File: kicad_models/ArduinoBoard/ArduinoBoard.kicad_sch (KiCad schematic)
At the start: 21 parts, among them J1 5V Output, J2 Buttons, J3 PWM Output, J4 12V Input, J5 Conn_01x04_Pin, J6 Conn_01x04_Pin, J7 Conn_01x06_Pin, J8 Conn_01x06_Pin, J9 Position Input, SW1 SW_Push_Dual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

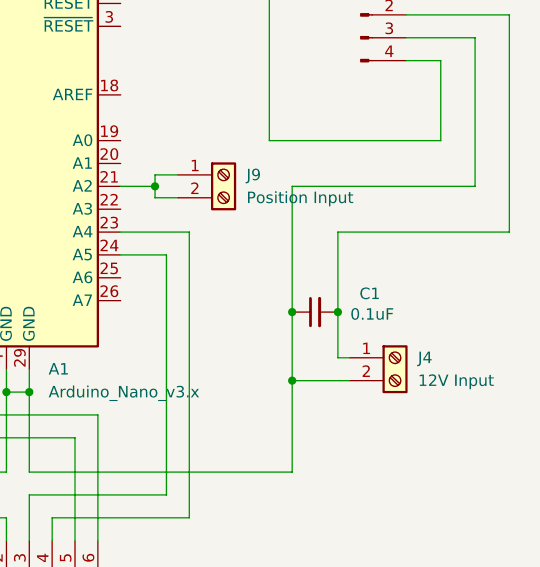
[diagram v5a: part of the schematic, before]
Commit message: Learned that adding a capacitor could actually make the surge worse. Changed to a Negative Temperature Coeficient (NTC) Thermistor instead. The thermistor adds resistance when cool and heats up with use, softening the surge to the buck converter.
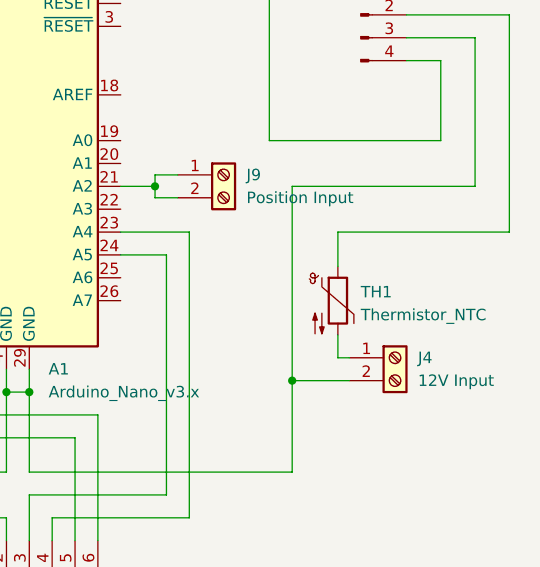
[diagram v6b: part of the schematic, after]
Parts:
- removed C1: 0.1uF, Capacitor_THT:C_Disc_D3.0mm_W2.0mm_P2.50mm, symbol Device:C_Small
- added TH1: Thermistor_NTC, Resistor_THT:R_Axial_DIN0204_L3.6mm_D1.6mm_P5.08mm_Vertical, symbol Device:Thermistor_NTC
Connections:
- net at J5.2 (Pin_2): now also TH1.1; no longer J4.1 (Pin_1)
- new net: J4.1 (Pin_1), TH1.2
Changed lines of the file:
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@@
-	)
-	(junction
-		(at 163.83 113.03)
-		(diameter 0)
-		(color 0 0 0 0)
 	)
 	(junction
@@
 	)
 	(junction
-		(at 168.91 113.03)
-		(diameter 0)
-		(color 0 0 0 0)
-	)
-	(junction
 		(at 132.08 121.92)
 		(diameter 0)
@@
 	(wire
 		(pts
-			(xy 163.83 99.06) (xy 163.83 113.03)
-		)
-		(stroke
-			(width 0)
-			(type default)
-		)
-	)
-	(wire
-		(pts
 			(xy 161.29 66.04) (xy 129.54 66.04)
 		)
@@
 	(wire
 		(pts
-			(xy 168.91 104.14) (xy 168.91 113.03)
-		)
-		(stroke
-			(width 0)
-			(type default)
-		)
-	)
-	(wire
-		(pts
 			(xy 137.16 135.89) (xy 152.4 135.89)
 		)
@@
 	(wire
 		(pts
+			(xy 168.91 115.57) (xy 168.91 118.11)
+		)
+		(stroke
+			(width 0)
+			(type default)
+		)
+	)
+	(wire
+		(pts
 			(xy 149.86 106.68) (xy 144.78 106.68)
 		)
@@
 	(wire
 		(pts
-			(xy 168.91 113.03) (xy 168.91 118.11)
-		)
-		(stroke
-			(width 0)
-			(type default)
-		)
-	)
-	(wire
-		(pts
 			(xy 134.62 133.35) (xy 134.62 138.43)
 		)
@@
 	(wire
 		(pts
+			(xy 168.91 104.14) (xy 168.91 107.95)
+		)
+		(stroke
+			(width 0)
+			(type default)
+		)
+	)
+	(wire
+		(pts
 			(xy 115.57 57.15) (xy 137.16 57.15)
 		)
@@
 	(wire
 		(pts
-			(xy 163.83 113.03) (xy 163.83 120.65)
+			(xy 163.83 99.06) (xy 163.83 120.65)
 		)
 		(stroke
@@
 	)
 	(symbol
+		(lib_id "Device:Thermistor_NTC")
+		(at 168.91 111.76 0)
+		(unit 1)
+		(exclude_from_sim no)
+		(in_bom yes)
+		(on_board yes)
+		(dnp no)
+		(fields_autoplaced yes)
+		(property "Reference" "TH1"
+			(at 171.45 110.8074 0)
+			(effects
+				(font
+					(size 1.27 1.27)
+				)
+				(justify left)
+			)
+		)
+		(property "Value" "Thermistor_NTC"
+			(at 171.45 113.3474 0)
+			(effects
+				(font
+					(size 1.27 1.27)
+				)
+				(justify left)
+			)
+		)
+		(property "Footprint" "Resistor_THT:R_Axial_DIN0204_L3.6mm_D1.6mm_P5.08mm_Vertical"
+			(at 168.91 110.49 0)
+			(effects
+				(font
+					(size 1.27 1.27)
+				)
+				(hide yes)
+			)
+		)
+		(property "Datasheet" "~"
+			(at 168.91 110.49 0)
+			(effects
+				(font
+					(size 1.27 1.27)
+				)
+				(hide yes)
+			)
+		)
+		(property "Description" "Temperature dependent resistor, negative temperature coefficient"
+			(at 168.91 111.76 0)
+			(effects
+				(font
+					(size 1.27 1.27)
+				)
+				(hide yes)
+			)
+		)
+		(pin "2"
+		)
+		(pin "1"
+		)
+		(instances
+			(project ""
+				(path "/98bf385f-4cd5-4c0c-bda4-6735edf00281"
+					(reference "TH1")
+					(unit 1)
+				)
+			)
+		)
+	)
+	(symbol
 		(lib_id "Mechanical:MountingHole")
 		(at 158.75 191.77 0)
@@
 					(unit 1)
 				)
-			)
-		)
-	)
-	(symbol
-		(lib_id "Device:C_Small")
-		(at 166.37 113.03 90)
-		(unit 1)
-		(exclude_from_sim no)
-		(in_bom yes)
-		(on_board yes)
-		(dnp no)
-		(property "Reference" "C1"
-			(at 172.466 110.998 90)
-			(effects
-				(font
-					(size 1.27 1.27)
-				)
-			)
-		)
-		(property "Value" "0.1uF"
-			(at 172.72 113.284 90)
-			(effects
-				(font
-					(size 1.27 1.27)
-				)
-			)
-		)
-		(property "Footprint" "Capacitor_THT:C_Disc_D3.0mm_W2.0mm_P2.50mm"
-			(at 166.37 113.03 0)
-			(effects
-				(font
-					(size 1.27 1.27)
-				)
-				(hide yes)
-			)
-		)
-		(property "Datasheet" "~"
-			(at 166.37 113.03 0)
-			(effects
-				(font
-					(size 1.27 1.27)
-				)
-				(hide yes)
-			)
-		)
-		(property "Description" "Unpolarized capacitor, small symbol"
-			(at 166.37 113.03 0)
-			(effects
-				(font
-					(size 1.27 1.27)
-				)
-				(hide yes)
-			)
-		)
-		(pin "2"
-		)
-		(pin "1"
-		)
-		(instances
-			(project ""
-				(path "/98bf385f-4cd5-4c0c-bda4-6735edf00281"
-					(reference "C1")
-					(unit 1)
-				)

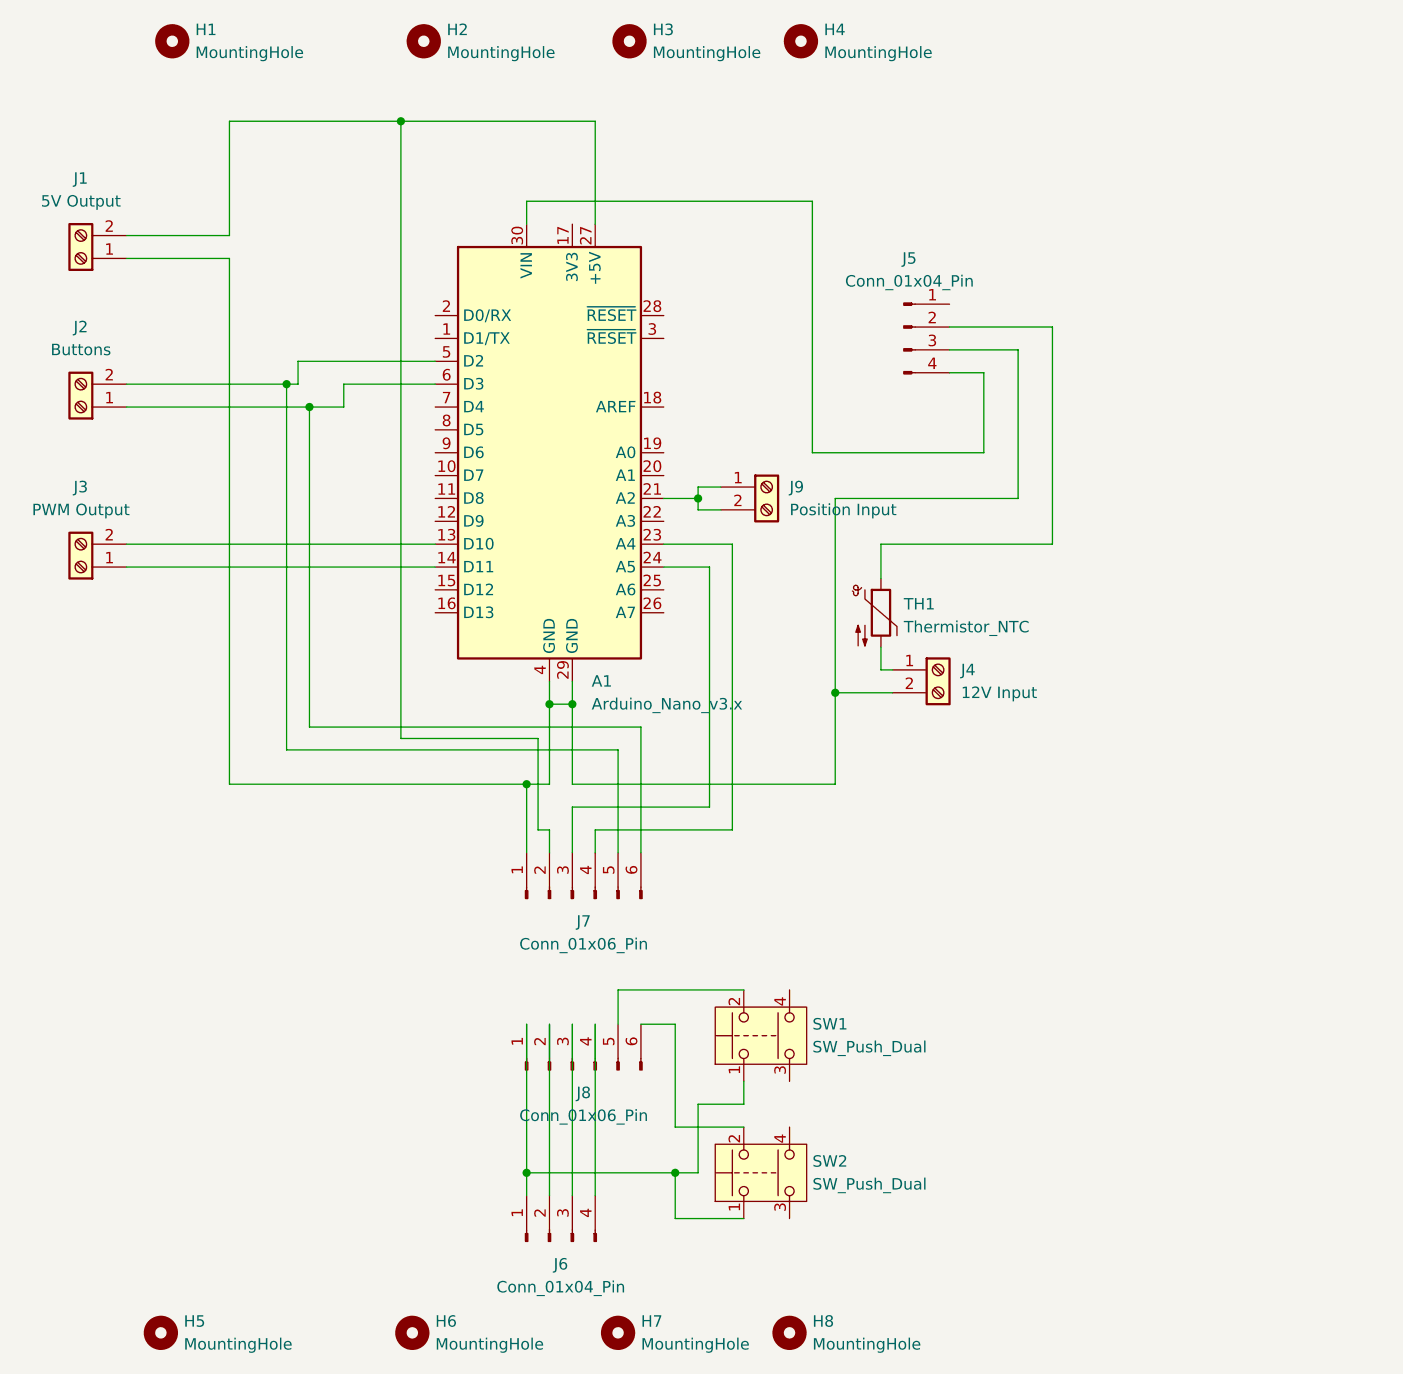
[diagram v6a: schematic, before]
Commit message: Made some pretty significant changes to the PCB layout. Removed the need for a via path to cross over a couple of tracks.
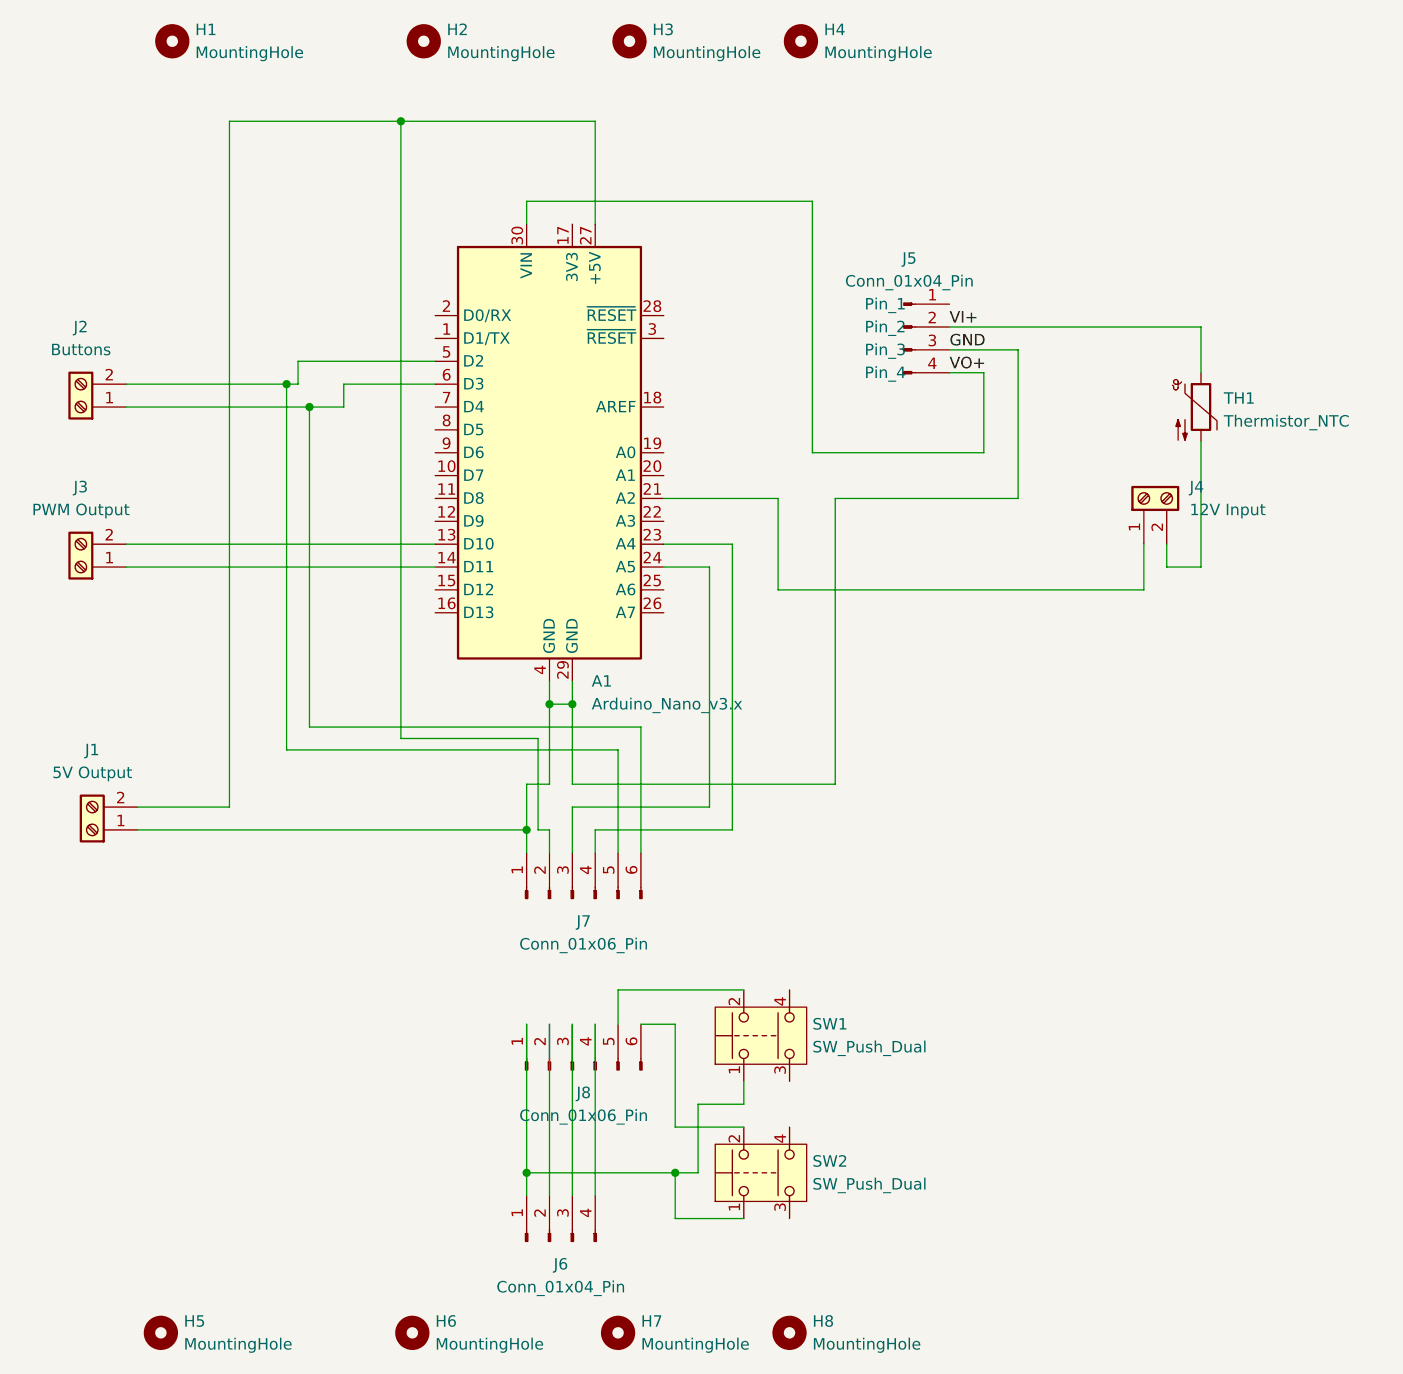
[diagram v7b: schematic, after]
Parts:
- removed J9: Position Input, TerminalBlock:TerminalBlock_bornier-2_P5.08mm, symbol Connector:Screw_Terminal_01x02
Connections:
- net VI+: now reaches J5.2 (Pin_2), TH1.1
- net at TH1.2: now also J4.2 (Pin_2); no longer J4.1 (Pin_1)
- net GND: now reaches A1.29 (GND), A1.4 (GND), J1.1 (Pin_1), J5.3 (Pin_3), J7.1 (Pin_1)
- net GND: no longer J4.2 (Pin_2)
- net at A1.21 (A2): now also J4.1 (Pin_1)
- net VO+: now reaches A1.30 (VIN), J5.4 (Pin_4)
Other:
- moved on the sheet: J1, J4, TH1

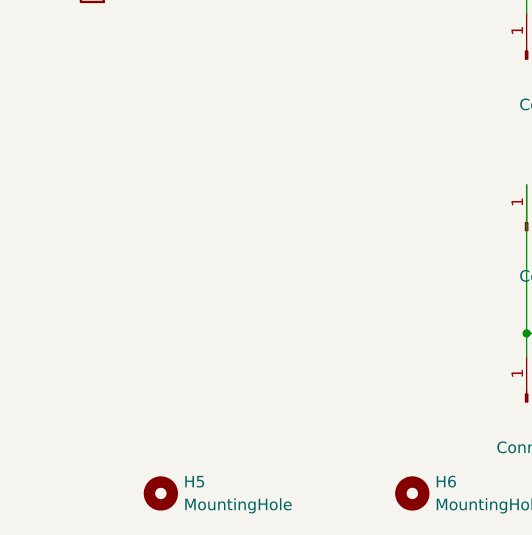
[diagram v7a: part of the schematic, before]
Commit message: Started to make a 3D printable face plate with Solid Edge. Also added another child board (OLED) that allows a hole to be drilled for a 12mm momentary on-off-on switch (rather than buttons) - this update requires the user so wire the switch with the screwdown terminals rather than with traces on the board. The parent board (Arduino) didn't change apart from scooting the Arduino to one side slightly to make room for the back of the switch.
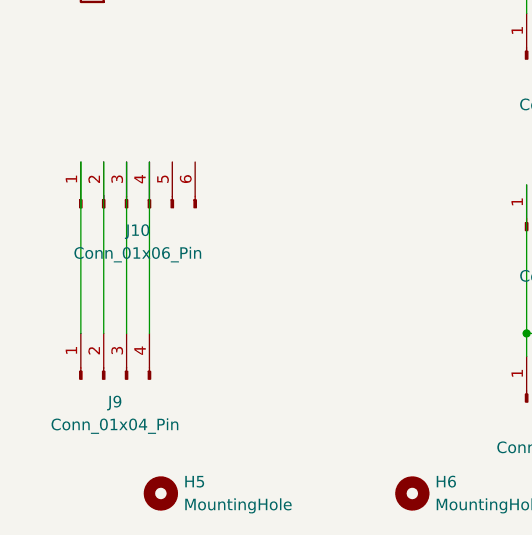
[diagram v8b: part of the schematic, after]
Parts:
- added J10: Conn_01x06_Pin, Connector_PinHeader_2.54mm:PinHeader_1x06_P2.54mm_Vertical, symbol Connector:Conn_01x06_Pin
- added J9: Conn_01x04_Pin, Connector_PinHeader_2.54mm:PinHeader_1x04_P2.54mm_Vertical, symbol Connector:Conn_01x04_Pin
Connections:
- new net: J10.1 (Pin_1), J9.1 (Pin_1)
- new net: J10.2 (Pin_2), J9.2 (Pin_2)
- new net: J10.3 (Pin_3), J9.3 (Pin_3)
- new net: J10.4 (Pin_4), J9.4 (Pin_4)
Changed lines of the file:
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@@
+	(wire
+		(pts
+			(xy 82.55 154.94) (xy 82.55 173.99)
+		)
+		(stroke
+			(width 0)
+			(type default)
+		)
+	)
 	(wire
 		(pts
@@
 	(wire
 		(pts
+			(xy 87.63 154.94) (xy 87.63 173.99)
+		)
+		(stroke
+			(width 0)
+			(type default)
+		)
+	)
+	(wire
+		(pts
+			(xy 80.01 154.94) (xy 80.01 173.99)
+		)
+		(stroke
+			(width 0)
+			(type default)
+		)
+	)
+	(wire
+		(pts
 			(xy 129.54 135.89) (xy 129.54 138.43)
 		)
@@
 		(pts
 			(xy 102.87 86.36) (xy 104.14 86.36)
+		)
+		(stroke
+			(width 0)
+			(type default)
+		)
+	)
+	(wire
+		(pts
+			(xy 85.09 154.94) (xy 85.09 173.99)
 		)
 		(stroke
@@
 					(unit 1)
 				)
+			)
+		)
+	)
+	(symbol
+		(lib_id "Connector:Conn_01x06_Pin")
+		(at 85.09 160.02 90)
+		(unit 1)
+		(exclude_from_sim no)
+		(in_bom yes)
+		(on_board yes)
+		(dnp no)
+		(fields_autoplaced yes)
+		(property "Reference" "J10"
+			(at 86.36 162.56 90)
+			(effects
+				(font
+					(size 1.27 1.27)
+				)
+			)
+		)
+		(property "Value" "Conn_01x06_Pin"
+			(at 86.36 165.1 90)
+			(effects
+				(font
+					(size 1.27 1.27)
+				)
+			)
+		)
+		(property "Footprint" "Connector_PinHeader_2.54mm:PinHeader_1x06_P2.54mm_Vertical"
+			(at 85.09 160.02 0)
+			(effects
+				(font
+					(size 1.27 1.27)
+				)
+				(hide yes)
+			)
+		)
+		(property "Datasheet" "~"
+			(at 85.09 160.02 0)
+			(effects
+				(font
+					(size 1.27 1.27)
+				)
+				(hide yes)
+			)
+		)
+		(property "Description" "Generic connector, single row, 01x06, script generated"
+			(at 85.09 160.02 0)
+			(effects
+				(font
+					(size 1.27 1.27)
+				)
+				(hide yes)
+			)
+		)
+		(pin "4"
+		)
+		(pin "5"
+		)
+		(pin "2"
+		)
+		(pin "6"
+		)
+		(pin "1"
+		)
+		(pin "3"
+		)
+		(instances
+			(project "ArduinoBoard"
+				(path "/98bf385f-4cd5-4c0c-bda4-6735edf00281"
+					(reference "J10")
+					(unit 1)
+				)
+			)
+		)
+	)
+	(symbol
+		(lib_id "Connector:Conn_01x04_Pin")
+		(at 82.55 179.07 90)
+		(unit 1)
+		(exclude_from_sim no)
+		(in_bom yes)
+		(on_board yes)
+		(dnp no)
+		(fields_autoplaced yes)
+		(property "Reference" "J9"
+			(at 83.82 181.61 90)
+			(effects
+				(font
+					(size 1.27 1.27)
+				)
+			)
+		)
+		(property "Value" "Conn_01x04_Pin"
+			(at 83.82 184.15 90)
+			(effects
+				(font
+					(size 1.27 1.27)
+				)
+			)
+		)
+		(property "Footprint" "Connector_PinHeader_2.54mm:PinHeader_1x04_P2.54mm_Vertical"
+			(at 82.55 179.07 0)
+			(effects
+				(font
+					(size 1.27 1.27)
+				)
+				(hide yes)
+			)
+		)
+		(property "Datasheet" "~"
+			(at 82.55 179.07 0)
+			(effects
+				(font
+					(size 1.27 1.27)
+				)
+				(hide yes)
+			)
+		)
+		(property "Description" "Generic connector, single row, 01x04, script generated"
+			(at 82.55 179.07 0)
+			(effects
+				(font
+					(size 1.27 1.27)
+				)
+				(hide yes)
+			)
+		)
+		(pin "2"
+		)
+		(pin "4"
+		)
+		(pin "3"
+		)
+		(pin "1"
+		)
+		(instances
+			(project "ArduinoBoard"
+				(path "/98bf385f-4cd5-4c0c-bda4-6735edf00281"
+					(reference "J9")
+					(unit 1)
+				)
